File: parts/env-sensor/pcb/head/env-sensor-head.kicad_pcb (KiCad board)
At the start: 2 copper layers, 40 x 18.3 mm, 10 parts

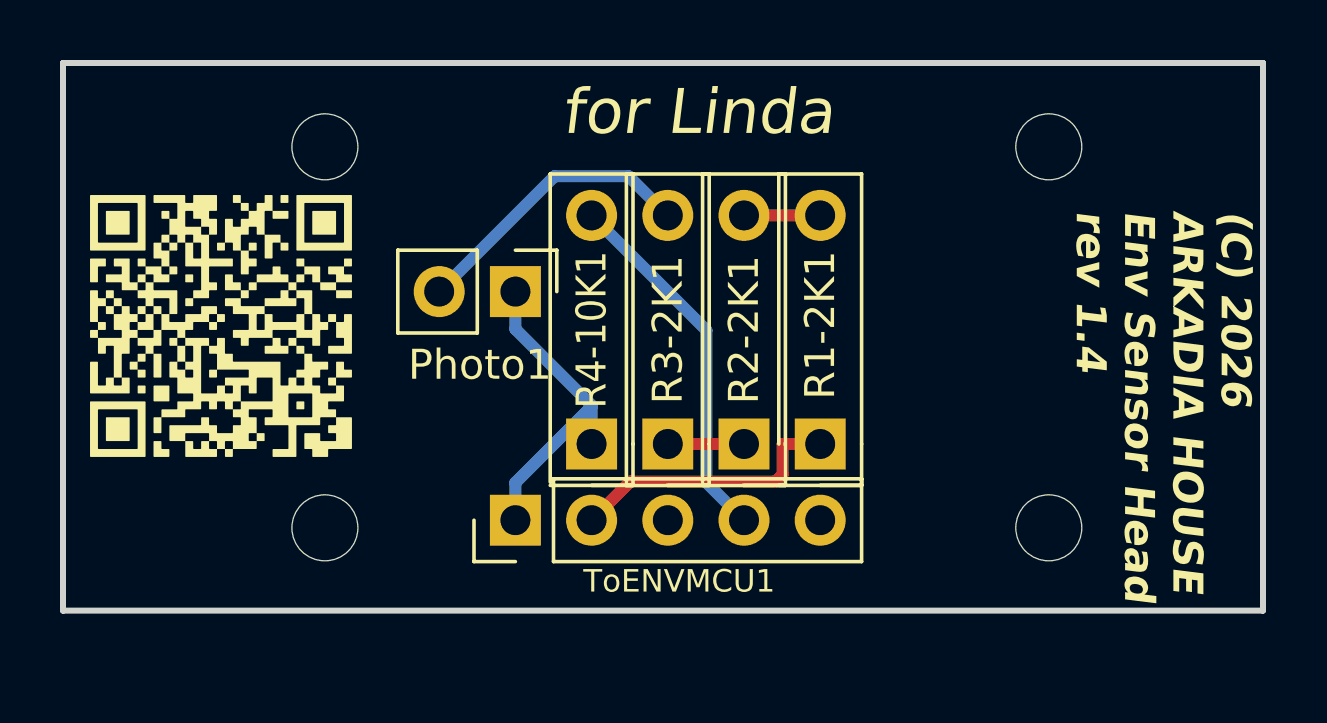
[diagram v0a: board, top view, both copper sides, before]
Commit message: rev QR code and update to KiCad 10
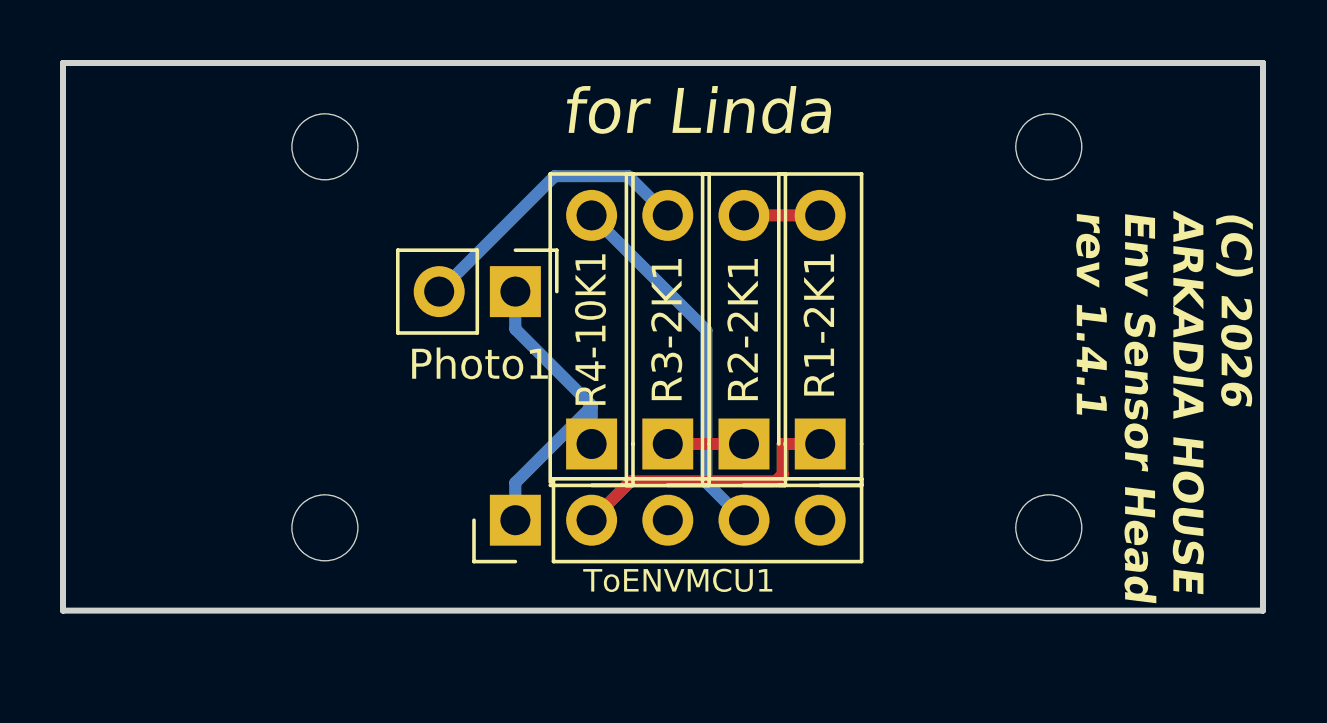
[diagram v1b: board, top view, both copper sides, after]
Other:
- board text added: "(C) 2026 ARKADIA HOUSE Env Sensor Head rev 1.4.1"
- board text removed: "(C) 2026 ARKADIA HOUSE Env Sensor Head rev 1.4"
